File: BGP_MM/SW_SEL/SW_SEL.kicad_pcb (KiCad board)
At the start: 2 copper layers, 17 x 13 mm, 2 parts, among them P1 CONN_01X04, SW1 Switch_SPDT_x2

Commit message: MM Tweaks
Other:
- board text added: "MM Sabre Sel Switch CBD Design"
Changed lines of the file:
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@@
     (links 6)
     (no_connects 0)
-    (area 136.924999 95.924999 150.075001 113.075001)
+    (area 136.924999 82.924999 154.075001 96.075001)
     (thickness 1.6)
-    (drawings 4)
+    (drawings 5)
     (tracks 13)
     (zones 0)
@@
     )
   )
+  (gr_text "MM Sabre\nSel Switch\nCBD Design" (at 138.8 87.5 270) (layer B.SilkS)
+    (effects (font (size 0.6 0.6) (thickness 0.15)))
+  )
   (gr_line (start 154 96) (end 137 96) (layer Edge.Cuts) (width 0.15))

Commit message: MM Switches and BOM
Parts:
- moved P1 1.00 mm to (150.7, 92.5)
- moved SW1 0.80 mm to (145.2, 84.8)
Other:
- board size 17 x 13 mm -> 16 x 13 mm
- board text added: "MM Sabre Sel Switch"
- board text removed: "MM Sabre Sel Switch CBD Design"
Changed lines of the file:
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@@
     (links 6)
     (no_connects 0)
-    (area 136.924999 82.924999 154.075001 96.075001)
+    (area 136.624999 82.574999 153.225001 96.225001)
     (thickness 1.6)
     (drawings 5)
-    (tracks 13)
+    (tracks 12)
     (zones 0)
     (modules 2)
@@
     (add_net Earth)
   )
-  (module LIBS:NKK_DPDT (layer F.Cu)
-    (at 146.0036 84.7989 90)
-    (descr "2-way 2.54mm pitch terminal block, Phoenix MPT series")
-    (fp_text reference SW1 (at -4.6011 -2.1036 270) (layer F.SilkS)
-      (effects (font (size 1 1) (thickness 0.15)))
-    )
-    (fp_text value Switch_SPDT_x2 (at -4.45 5.2 90) (layer F.Fab) hide
-      (effects (font (size 1 1) (thickness 0.15)))
-    )
-    (fp_text user %R (at -4.6011 -2.1036 90) (layer F.Fab) hide
-      (effects (font (size 1 1) (thickness 0.15)))
-    )
-    (fp_line (start 1.95 4.1) (end -11.35 4.1) (layer F.CrtYd) (width 0.05))
-    (fp_line (start 1.95 -8.9) (end 1.95 4.1) (layer F.CrtYd) (width 0.05))
-    (fp_line (start -11.346872 -8.899165) (end 1.95 -8.9) (layer F.CrtYd) (width 0.05))
-    (fp_line (start -11.35 4.1) (end -11.35 -8.9) (layer F.CrtYd) (width 0.05))
-    (fp_line (start 1.8 -8.75) (end -11.2 -8.75) (layer F.SilkS) (width 0.15))
-    (fp_line (start -11.2 -8.75) (end -11.2 3.95) (layer F.SilkS) (width 0.15))
-    (fp_line (start -11.2 3.95) (end 1.8 3.95) (layer F.SilkS) (width 0.15))
-    (fp_line (start 1.8 3.95) (end 1.8 -8.75) (layer F.SilkS) (width 0.15))
-    (pad 5 thru_hole oval (at -4.7 -4.8 270) (size 1.8 1.8) (drill 1) (layers *.Cu *.Mask)
-      (net 3 /JZ_I))
-    (pad 4 thru_hole circle (at 0 -4.8 270) (size 1.8 1.8) (drill 1) (layers *.Cu *.Mask)
-      (net 2 /SIG_O))
-    (pad 6 thru_hole oval (at -9.4 -4.8 270) (size 1.8 1.8) (drill 1) (layers *.Cu *.Mask)
-      (net 1 Earth))
-    (pad 1 thru_hole circle (at 0 0.03 270) (size 1.8 1.8) (drill 1) (layers *.Cu *.Mask)
-      (net 1 Earth))
-    (pad 2 thru_hole oval (at -4.7 0.03 270) (size 1.8 1.8) (drill 1) (layers *.Cu *.Mask)
-      (net 4 /MM_I))
-    (pad 3 thru_hole oval (at -9.4 0.03 270) (size 1.8 1.8) (drill 1) (layers *.Cu *.Mask)
-      (net 2 /SIG_O))
-    (model ${KISYS3DMOD}/TerminalBlock_Phoenix.3dshapes/TerminalBlock_Phoenix_MPT-2.54mm_2pol.wrl
-      (at (xyz 0.05 0 0))
-      (scale (xyz 1 1 1))
-      (rotate (xyz 0 0 0))
-    )
-  )
   (module Connectors_JST:JST_PH_B4B-PH-K_04x2.00mm_Straight (layer B.Cu)
-    (at 151.7 92.4 90)
+    (at 150.7 92.5 90)
     (descr "JST PH series connector, B4B-PH-K, top entry type, through hole, Datasheet: http://www.jst-mfg.com/product/pdf/eng/ePH.pdf")
     (tags "connector jst ph")
@@
     )
   )
-  (gr_text "MM Sabre\nSel Switch\nCBD Design" (at 138.8 87.5 270) (layer B.SilkS)
+  (module LIBS:NKK_DPDT (layer F.Cu)
+    (at 145.2 84.8 90)
+    (descr "2-way 2.54mm pitch terminal block, Phoenix MPT series")
+    (fp_text reference SW1 (at -5.1 -2.2 270) (layer F.SilkS)
+      (effects (font (size 1 1) (thickness 0.15)))
+    )
+    (fp_text value Switch_SPDT_x2 (at -4.45 4.55 90) (layer F.Fab) hide
+      (effects (font (size 1 1) (thickness 0.15)))
+    )
+    (fp_text user %R (at -5.1 -2.2 270) (layer F.Fab)
+      (effects (font (size 1 1) (thickness 0.15)))
+    )
+    (fp_line (start 1.8 3.45) (end -11.2 3.45) (layer F.CrtYd) (width 0.05))
+    (fp_line (start 1.8 -8.25) (end 1.8 3.45) (layer F.CrtYd) (width 0.05))
+    (fp_line (start -11.2 -8.25) (end 1.8 -8.25) (layer F.CrtYd) (width 0.05))
+    (fp_line (start -11.2 3.45) (end -11.2 -8.25) (layer F.CrtYd) (width 0.05))
+    (fp_line (start 1.65 -8.1) (end -11.05 -8.1) (layer F.SilkS) (width 0.15))
+    (fp_line (start -11.05 -8.1) (end -11.05 3.3) (layer F.SilkS) (width 0.15))
+    (fp_line (start -11.05 3.3) (end 1.65 3.3) (layer F.SilkS) (width 0.15))
+    (fp_line (start 1.65 3.3) (end 1.65 -8.1) (layer F.SilkS) (width 0.15))
+    (pad 5 thru_hole oval (at -4.7 -4.8 270) (size 1.8 1.8) (drill 1) (layers *.Cu *.Mask)
+      (net 3 /JZ_I))
+    (pad 4 thru_hole circle (at 0 -4.8 270) (size 1.8 1.8) (drill 1) (layers *.Cu *.Mask)
+      (net 2 /SIG_O))
+    (pad 6 thru_hole oval (at -9.4 -4.8 270) (size 1.8 1.8) (drill 1) (layers *.Cu *.Mask)
+      (net 1 Earth))
+    (pad 1 thru_hole circle (at 0 0.03 270) (size 1.8 1.8) (drill 1) (layers *.Cu *.Mask)
+      (net 1 Earth))
+    (pad 2 thru_hole oval (at -4.7 0.03 270) (size 1.8 1.8) (drill 1) (layers *.Cu *.Mask)
+      (net 4 /MM_I))
+    (pad 3 thru_hole oval (at -9.4 0.03 270) (size 1.8 1.8) (drill 1) (layers *.Cu *.Mask)
+      (net 2 /SIG_O))
+    (model ${KISYS3DMOD}/TerminalBlock_Phoenix.3dshapes/TerminalBlock_Phoenix_MPT-2.54mm_2pol.wrl
+      (at (xyz 0.05 0 0))
+      (scale (xyz 1 1 1))
+      (rotate (xyz 0 0 0))
+    )
+  )
+  (gr_text "MM Sabre\nSel Switch" (at 138.3 87.5 270) (layer B.SilkS)
     (effects (font (size 0.6 0.6) (thickness 0.15)))
   )
-  (gr_line (start 154 96) (end 137 96) (layer Edge.Cuts) (width 0.15))
-  (gr_line (start 154 83) (end 154 96) (layer Edge.Cuts) (width 0.15))
-  (gr_line (start 137 83) (end 154 83) (layer Edge.Cuts) (width 0.15))
+  (gr_line (start 153 96) (end 137 96) (layer Edge.Cuts) (width 0.15))
+  (gr_line (start 153 83) (end 153 96) (layer Edge.Cuts) (width 0.15))
+  (gr_line (start 137 83) (end 153 83) (layer Edge.Cuts) (width 0.15))
   (gr_line (start 137 96) (end 137 83) (layer Edge.Cuts) (width 0.15))
-  (segment (start 146.0336 94.1989) (end 143.8 91.9653) (width 0.5) (layer F.Cu) (net 2))
-  (segment (start 143.8 91.9653) (end 143.8 87.3953) (width 0.5) (layer F.Cu) (net 2))
-  (segment (start 143.8 87.3953) (end 142.103599 85.698899) (width 0.5) (layer F.Cu) (net 2))
-  (segment (start 142.103599 85.698899) (end 141.2036 84.7989) (width 0.5) (layer F.Cu) (net 2))
-  (segment (start 151.7 90.4) (end 149.8325 90.4) (width 0.5) (layer F.Cu) (net 2))
-  (segment (start 149.8325 90.4) (end 146.933599 93.298901) (width 0.5) (layer F.Cu) (net 2))
-  (segment (start 146.933599 93.298901) (end 146.0336 94.1989) (width 0.5) (layer F.Cu) (net 2))
-  (segment (start 143.4025 87.3) (end 141.2036 89.4989) (width 0.5) (layer B.Cu) (net 3))
-  (segment (start 150.35 88.4) (end 149.25 87.3) (width 0.5) (layer B.Cu) (net 3))
-  (segment (start 149.25 87.3) (end 143.4025 87.3) (width 0.5) (layer B.Cu) (net 3))
-  (segment (start 151.7 88.4) (end 150.35 88.4) (width 0.5) (layer B.Cu) (net 3))
-  (segment (start 151.7 86.4) (end 149.1325 86.4) (width 0.5) (layer F.Cu) (net 4))
-  (segment (start 149.1325 86.4) (end 146.0336 89.4989) (width 0.5) (layer F.Cu) (net 4))
+  (segment (start 140.4 84.8) (end 143 87.4) (width 0.5) (layer F.Cu) (net 2))
+  (segment (start 144.330001 93.300001) (end 145.23 94.2) (width 0.5) (layer F.Cu) (net 2))
+  (segment (start 143 87.4) (end 143 91.97) (width 0.5) (layer F.Cu) (net 2))
+  (segment (start 143 91.97) (end 144.330001 93.300001) (width 0.5) (layer F.Cu) (net 2))
+  (segment (start 150.7 90.5) (end 148.93 90.5) (width 0.5) (layer F.Cu) (net 2))
+  (segment (start 148.93 90.5) (end 145.23 94.2) (width 0.5) (layer F.Cu) (net 2))
+  (segment (start 147.85 87) (end 142.9 87) (width 0.5) (layer B.Cu) (net 3))
+  (segment (start 142.9 87) (end 140.4 89.5) (width 0.5) (layer B.Cu) (net 3))
+  (segment (start 150.7 88.5) (end 149.35 88.5) (width 0.5) (layer B.Cu) (net 3))
+  (segment (start 149.35 88.5) (end 147.85 87) (width 0.5) (layer B.Cu) (net 3))
+  (segment (start 150.7 86.5) (end 148.23 86.5) (width 0.5) (layer F.Cu) (net 4))
+  (segment (start 148.23 86.5) (end 145.23 89.5) (width 0.5) (layer F.Cu) (net 4))
   (zone (net 1) (net_name Earth) (layer F.Cu) (hatch edge 0.508)
     (connect_pads (clearance 0.3))
@@
     (polygon
       (pts
-        (xy 137 96) (xy 137 83) (xy 154 83) (xy 154 96)
+        (xy 137 96) (xy 137 83) (xy 153 83) (xy 153 96)
       )
     )
@@
     (polygon
       (pts
-        (xy 137 96) (xy 137 83) (xy 154 83) (xy 154 96)
+        (xy 137 96) (xy 137 83) (xy 153 83) (xy 153 96)
       )
     )

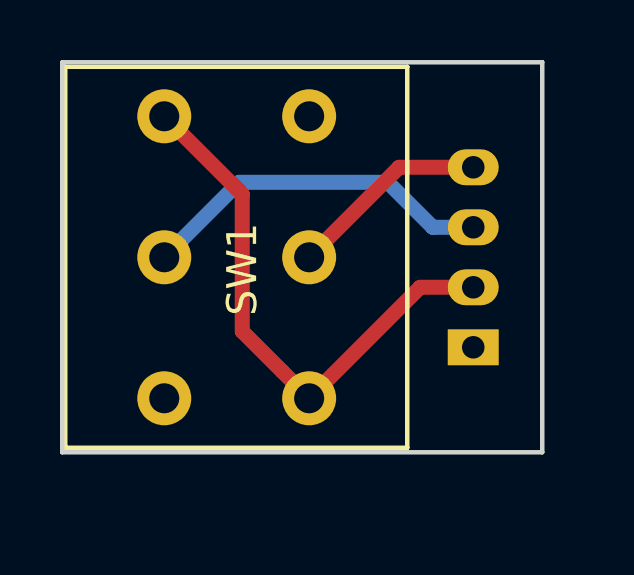
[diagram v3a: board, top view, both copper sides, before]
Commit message: MM Switch Config Changed
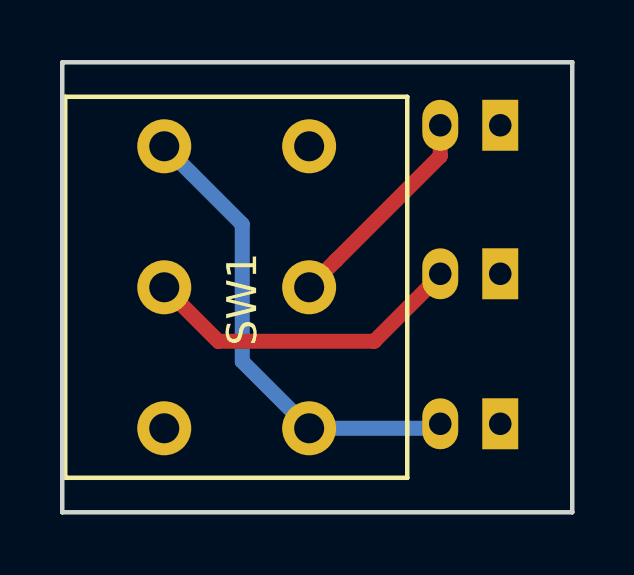
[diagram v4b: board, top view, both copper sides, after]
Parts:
- removed P1: CONN_01X04, Connectors_JST:JST_PH_B4B-PH-K_04x2.00mm_Straight
- added J1: Conn_01x02_Male, Connectors_JST:JST_PH_B2B-PH-K_02x2.00mm_Straight, B.Cu at (151.6, 85.1)
- added J2: Conn_01x02_Male, Connectors_JST:JST_PH_B2B-PH-K_02x2.00mm_Straight, B.Cu at (151.6, 90.0)
- added J3: Conn_01x02_Male, Connectors_JST:JST_PH_B2B-PH-K_02x2.00mm_Straight, B.Cu at (151.6, 95.0)
- moved SW1 1.00 mm to (145.2, 85.8)
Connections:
- SW1 pad 2: /MM_I -> /I_BR
- SW1 pad 5: /JZ_I -> /I_NK
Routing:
- net /JZ_I: track 12.0 -> 0.00 mm
- net /I_NK: track 0.00 -> 10.9 mm
- net /I_BR: track 0.00 -> 7.21 mm
- net /MM_I: track 6.71 -> 0.00 mm
- net /SIG_O: track 18.4 -> 15.8 mm
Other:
- board size 16 x 13 mm -> 17 x 15 mm

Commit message: MM Switch
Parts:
- removed J3: Conn_01x02_Male, Connectors_JST:JST_PH_B2B-PH-K_02x2.00mm_Straight
- J1: value Conn_01x02_Male -> CONN_01X03; footprint Connectors_JST:JST_PH_B2B-PH-K_02x2.00mm_Straight -> Connectors_JST:JST_PH_B3B-PH-K_03x2.00mm_Straight
- moved J2 5.83 mm to (149.8, 95.6), turned to 90 degrees
- moved J1 4.39 mm to (149.8, 89.1), turned to 90 degrees
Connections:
- J2 pad 2: /I_NK -> /SIG_O
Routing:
- net /I_BR: track 7.21 -> 5.98 mm
- net /SIG_O: track 15.8 -> 16.6 mm
- net /I_NK: track 10.9 -> 11.6 mm
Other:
- board size 17 x 15 mm -> 15 x 15 mm

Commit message: MM Refactoring
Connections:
- net /SIG_O renamed /SEL_O
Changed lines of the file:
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@@
     (links 7)
     (no_connects 0)
-    (area 136.924999 82.924999 154.075001 98.075001)
+    (area 136.924999 82.924999 152.075001 98.075001)
     (thickness 1.6)
     (drawings 5)
@@
   (net 0 "")
   (net 1 Earth)
-  (net 2 /SIG_O)
-  (net 3 /I_BR)
-  (net 4 /I_NK)
+  (net 2 /I_BR)
+  (net 3 /I_NK)
+  (net 4 /SEL_O)
   (net_class Default "This is the default net class."
     (clearance 0.3)
@@
     (add_net /I_BR)
     (add_net /I_NK)
-    (add_net /SIG_O)
+    (add_net /SEL_O)
     (add_net Earth)
   )
@@
     (fp_line (start 1.65 3.3) (end 1.65 -8.1) (layer F.SilkS) (width 0.15))
     (pad 5 thru_hole oval (at -4.7 -4.8 270) (size 1.8 1.8) (drill 1) (layers *.Cu *.Mask)
-      (net 4 /I_NK))
+      (net 3 /I_NK))
     (pad 4 thru_hole circle (at 0 -4.8 270) (size 1.8 1.8) (drill 1) (layers *.Cu *.Mask)
-      (net 2 /SIG_O))
+      (net 4 /SEL_O))
     (pad 6 thru_hole oval (at -9.4 -4.8 270) (size 1.8 1.8) (drill 1) (layers *.Cu *.Mask)
       (net 1 Earth))
@@
       (net 1 Earth))
     (pad 2 thru_hole oval (at -4.7 0.03 270) (size 1.8 1.8) (drill 1) (layers *.Cu *.Mask)
-      (net 3 /I_BR))
+      (net 2 /I_BR))
     (pad 3 thru_hole oval (at -9.4 0.03 270) (size 1.8 1.8) (drill 1) (layers *.Cu *.Mask)
-      (net 2 /SIG_O))
+      (net 4 /SEL_O))
     (model ${KISYS3DMOD}/TerminalBlock_Phoenix.3dshapes/TerminalBlock_Phoenix_MPT-2.54mm_2pol.wrl
       (at (xyz 0.05 0 0))
@@
       (net 1 Earth))
     (pad 2 thru_hole oval (at 2 0 90) (size 1.2 1.7) (drill 0.75) (layers *.Cu *.Mask)
-      (net 3 /I_BR))
+      (net 2 /I_BR))
     (pad 3 thru_hole oval (at 4 0 90) (size 1.2 1.7) (drill 0.75) (layers *.Cu *.Mask)
-      (net 4 /I_NK))
+      (net 3 /I_NK))
     (model ${KISYS3DMOD}/Connectors_JST.3dshapes/JST_PH_B3B-PH-K_03x2.00mm_Straight.wrl
       (at (xyz 0 0 0))
@@
       (net 1 Earth))
     (pad 2 thru_hole oval (at 2 0 90) (size 1.2 1.7) (drill 0.75) (layers *.Cu *.Mask)
-      (net 2 /SIG_O))
+      (net 4 /SEL_O))
     (model ${KISYS3DMOD}/Connectors_JST.3dshapes/JST_PH_B2B-PH-K_02x2.00mm_Straight.wrl
       (at (xyz 0 0 0))
@@
   (gr_line (start 137 83) (end 152 83) (layer Edge.Cuts) (width 0.15))
   (gr_line (start 137 98) (end 137 83) (layer Edge.Cuts) (width 0.15))
-  (segment (start 145.23 95.2) (end 142.8 92.77) (width 0.5) (layer B.Cu) (net 2))
-  (segment (start 142.8 92.77) (end 142.8 88.2) (width 0.5) (layer B.Cu) (net 2))
-  (segment (start 142.8 88.2) (end 141.299999 86.699999) (width 0.5) (layer B.Cu) (net 2))
-  (segment (start 141.299999 86.699999) (end 140.4 85.8) (width 0.5) (layer B.Cu) (net 2))
-  (segment (start 149.8 93.6) (end 146.83 93.6) (width 0.5) (layer B.Cu) (net 2))
-  (segment (start 146.83 93.6) (end 145.23 95.2) (width 0.5) (layer B.Cu) (net 2))
-  (segment (start 149.8 87.1) (end 148.63 87.1) (width 0.5) (layer F.Cu) (net 3))
-  (segment (start 148.63 87.1) (end 146.129999 89.600001) (width 0.5) (layer F.Cu) (net 3))
-  (segment (start 146.129999 89.600001) (end 145.23 90.5) (width 0.5) (layer F.Cu) (net 3))
-  (segment (start 149.8 85.1) (end 148.45 85.1) (width 0.5) (layer F.Cu) (net 4))
-  (segment (start 148.45 85.1) (end 143.05 90.5) (width 0.5) (layer F.Cu) (net 4))
-  (segment (start 143.05 90.5) (end 141.672792 90.5) (width 0.5) (layer F.Cu) (net 4))
-  (segment (start 141.672792 90.5) (end 140.4 90.5) (width 0.5) (layer F.Cu) (net 4))
+  (segment (start 149.8 87.1) (end 148.63 87.1) (width 0.5) (layer F.Cu) (net 2))
+  (segment (start 148.63 87.1) (end 146.129999 89.600001) (width 0.5) (layer F.Cu) (net 2))
+  (segment (start 146.129999 89.600001) (end 145.23 90.5) (width 0.5) (layer F.Cu) (net 2))
+  (segment (start 149.8 85.1) (end 148.45 85.1) (width 0.5) (layer F.Cu) (net 3))
+  (segment (start 148.45 85.1) (end 143.05 90.5) (width 0.5) (layer F.Cu) (net 3))
+  (segment (start 143.05 90.5) (end 141.672792 90.5) (width 0.5) (layer F.Cu) (net 3))
+  (segment (start 141.672792 90.5) (end 140.4 90.5) (width 0.5) (layer F.Cu) (net 3))
+  (segment (start 145.23 95.2) (end 142.8 92.77) (width 0.5) (layer B.Cu) (net 4))
+  (segment (start 142.8 92.77) (end 142.8 88.2) (width 0.5) (layer B.Cu) (net 4))
+  (segment (start 142.8 88.2) (end 141.299999 86.699999) (width 0.5) (layer B.Cu) (net 4))
+  (segment (start 141.299999 86.699999) (end 140.4 85.8) (width 0.5) (layer B.Cu) (net 4))
+  (segment (start 149.8 93.6) (end 146.83 93.6) (width 0.5) (layer B.Cu) (net 4))
+  (segment (start 146.83 93.6) (end 145.23 95.2) (width 0.5) (layer B.Cu) (net 4))
   (zone (net 1) (net_name Earth) (layer F.Cu) (hatch edge 0.508)
     (connect_pads (clearance 0.3))

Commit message: MM Refactoring
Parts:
- J1: value CONN_01X03 -> Conn_01x03_Male; footprint Connectors_JST:JST_PH_B3B-PH-K_03x2.00mm_Straight -> Pin_Headers:Pin_Header_Straight_1x03_Pitch2.54mm; moved to F.Cu
- J2: footprint Connectors_JST:JST_PH_B2B-PH-K_02x2.00mm_Straight -> Pin_Headers:Pin_Header_Straight_1x02_Pitch2.54mm; moved to F.Cu
- SW1: moved to B.Cu
- moved SW1 9.40 mm to (145.2, 95.2), turned to 270 degrees
- moved J1 3.79 mm to (150.1, 85.3), turned to 0 degrees
- moved J2 2.56 mm to (150.1, 93.1), turned to 0 degrees
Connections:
- J1 pad 1: Earth -> /I_NK
- J1 pad 3: /I_NK -> Earth
- J2 pad 1: Earth -> /SEL_O
- J2 pad 2: /SEL_O -> Earth
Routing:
- net /SEL_O: track 16.6 -> 19.0 mm
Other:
- board size 15 x 15 mm -> 15 x 13 mm
- board text removed: "MM Sabre Sel Switch"
